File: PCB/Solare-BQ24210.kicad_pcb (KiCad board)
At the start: 2 copper layers, 27.1 x 15.9 mm, 15 parts, among them J1 S2B-PH-K-S(LF)(SN), J2 S3B-PH-K-S(LF)(SN), J3 S2B-PH-K-S(LF)(SN), J4 S2B-PH-K-S(LF)(SN), U1 BQ24210DQCT

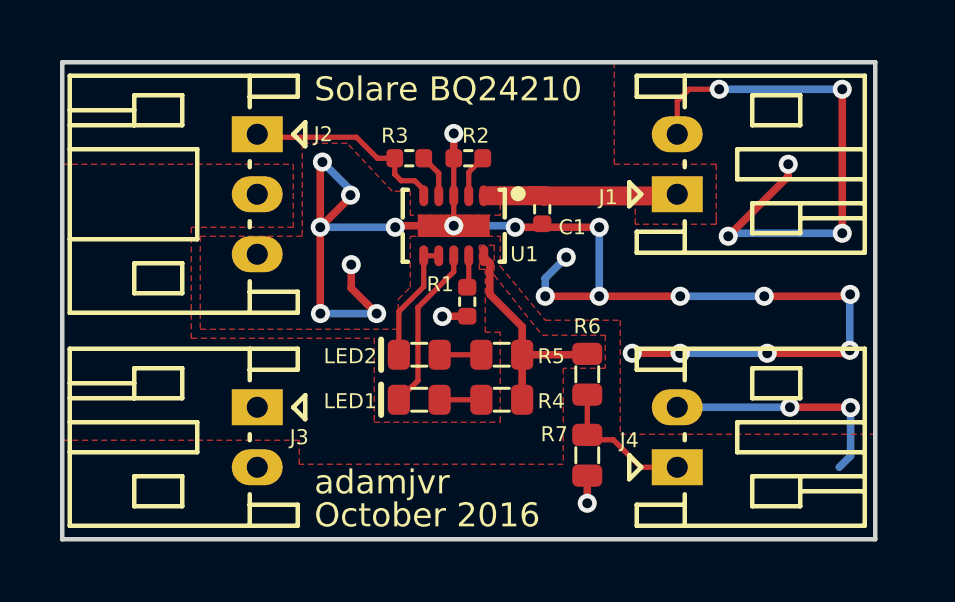
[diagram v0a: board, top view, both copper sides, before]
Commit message: ReadMe
Readme and pictures edited
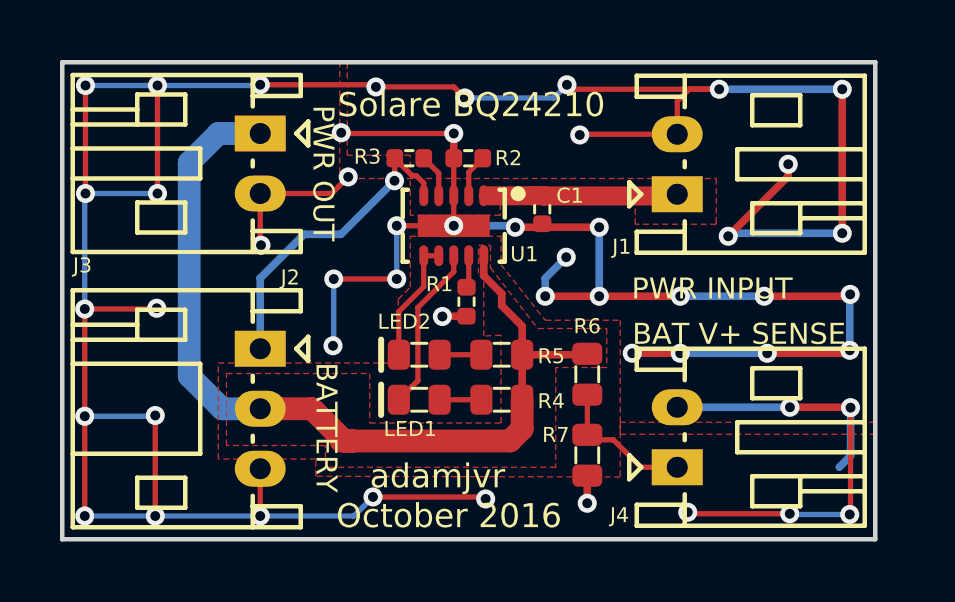
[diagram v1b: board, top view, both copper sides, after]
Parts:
- moved J3 9.13 mm to (57.3, 55.2)
- moved J2 7.15 mm to (57.3, 62.4)
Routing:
- net GND: track 76.0 -> 153.8 mm, vias 30 -> 51
- net /BAT: track 7.51 -> 31.6 mm
- net /THERM: track 6.83 -> 10.9 mm, vias 0 -> 1
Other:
- board text added: "BAT V+ SENSE"
- board text added: "BATTERY"
- board text added: "PWR INPUT"
- board text added: "PWR OUT"
- board text added: "Solare-BQ24210"
